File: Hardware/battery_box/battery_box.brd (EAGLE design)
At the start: 60 x 80.1 mm, 45 parts, among them IC1 AD826R, J1 CON_HEADER_PRG_PIC_ICSPA, Q1 IRFR5505PBFTO252, Q2 BSS123, X1 CON_MOLEX_39_29_1028, X2 KUSBVX

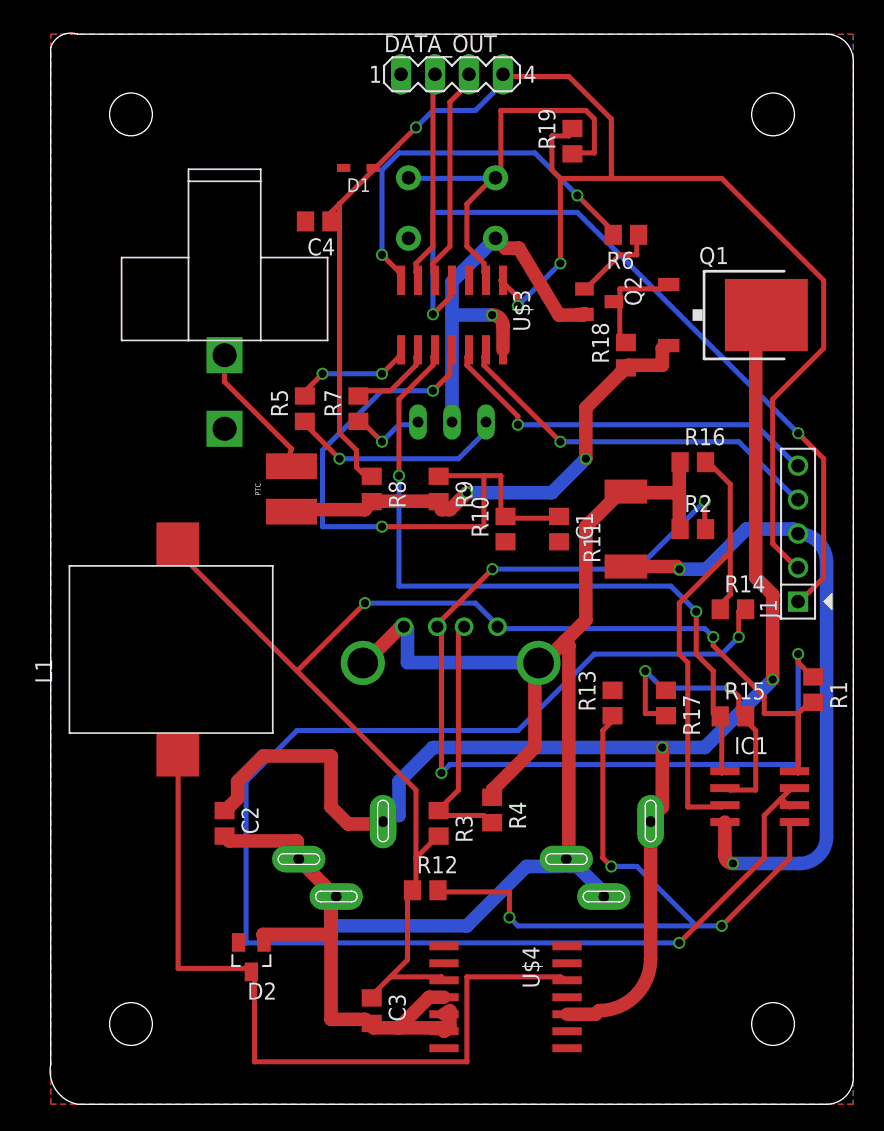
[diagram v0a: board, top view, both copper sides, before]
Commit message: Added new components with correct footprints
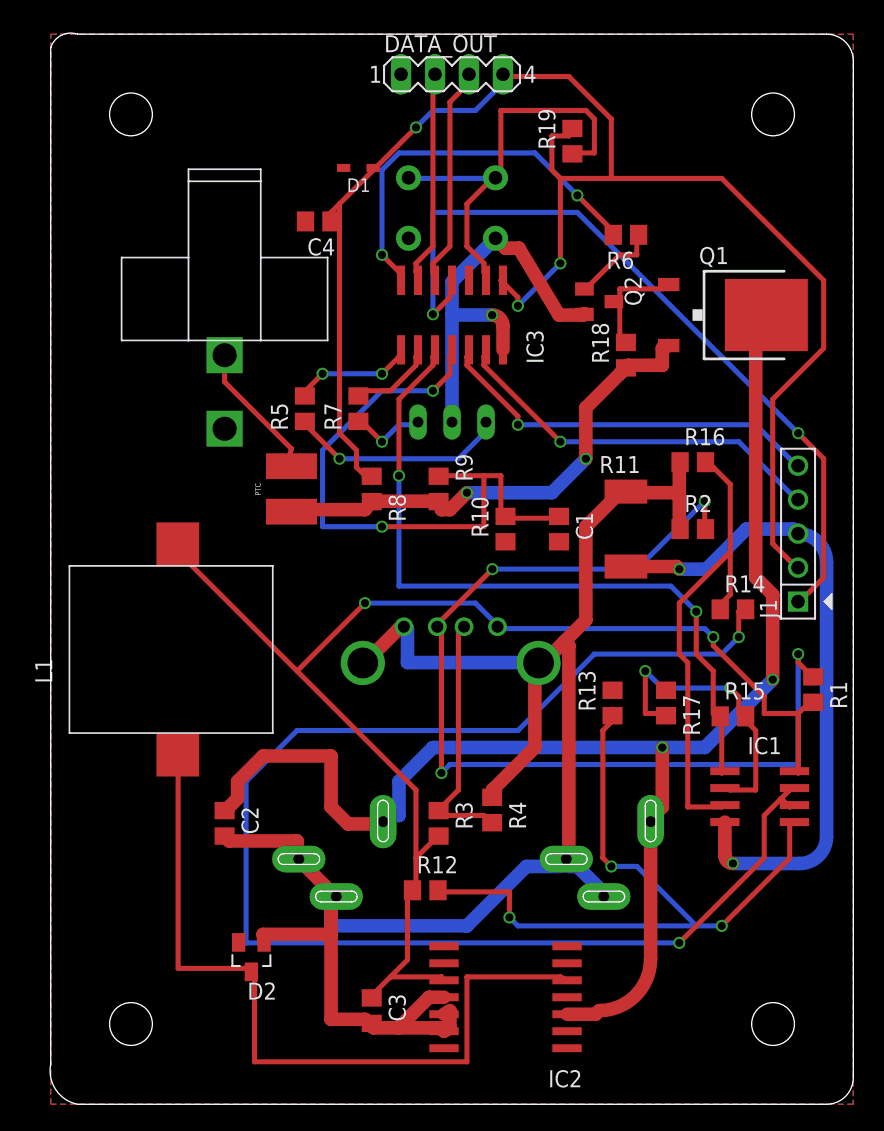
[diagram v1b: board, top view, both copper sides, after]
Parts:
- renumbered U$3 to IC3, U$4 to IC2
